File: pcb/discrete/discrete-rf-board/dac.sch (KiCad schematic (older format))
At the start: 19 parts, among them Q20 Q_NPN_BCE

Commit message: Autofill
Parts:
- C71, C72, C77, C78: footprint (none) -> Capacitor_SMD:C_0402_1005Metric; Mouser (none) -> 80-C0402C104M4P
- R45, R46, R47, R48: footprint (none) -> Resistor_SMD:R_0805_2012Metric_Pad1.15x1.40mm_HandSolder; Mouser (none) -> 71-CRCW080515K0FKEBC
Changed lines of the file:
@@
 F 0 "R55" V 3450 2800 50  0000 L CNN
 F 1 "15kR 1%" V 3550 2750 50  0000 L CNN
-F 2 "" H 3350 2850 50  0001 C CNN
+F 2 "Resistor_SMD:R_0805_2012Metric_Pad1.15x1.40mm_HandSolder" H 3350 2850 50  0001 C CNN
 F 3 "~" H 3350 2850 50  0001 C CNN
+F 4 "71-CRCW080515K0FKEBC" H 3350 2850 50  0001 C CNN "Mouser"
 	1    3350 2850
 	0    -1   1    0
@@
 F 0 "R56" V 3450 3100 50  0000 L CNN
 F 1 "15kR 1%" V 3550 3050 50  0000 L CNN
-F 2 "" H 3350 3150 50  0001 C CNN
+F 2 "Resistor_SMD:R_0805_2012Metric_Pad1.15x1.40mm_HandSolder" H 3350 3150 50  0001 C CNN
 F 3 "~" H 3350 3150 50  0001 C CNN
+F 4 "71-CRCW080515K0FKEBC" H 3350 3150 50  0001 C CNN "Mouser"
 	1    3350 3150
 	0    -1   1    0
@@
 F 0 "R57" V 3450 3400 50  0000 L CNN
 F 1 "15kR 1%" V 3550 3350 50  0000 L CNN
-F 2 "" H 3350 3450 50  0001 C CNN
+F 2 "Resistor_SMD:R_0805_2012Metric_Pad1.15x1.40mm_HandSolder" H 3350 3450 50  0001 C CNN
 F 3 "~" H 3350 3450 50  0001 C CNN
+F 4 "71-CRCW080515K0FKEBC" H 3350 3450 50  0001 C CNN "Mouser"
 	1    3350 3450
 	0    -1   1    0
@@
 F 0 "R58" V 3450 3700 50  0000 L CNN
 F 1 "15kR 1%" V 3550 3650 50  0000 L CNN
-F 2 "" H 3350 3750 50  0001 C CNN
+F 2 "Resistor_SMD:R_0805_2012Metric_Pad1.15x1.40mm_HandSolder" H 3350 3750 50  0001 C CNN
 F 3 "~" H 3350 3750 50  0001 C CNN
+F 4 "71-CRCW080515K0FKEBC" H 3350 3750 50  0001 C CNN "Mouser"
 	1    3350 3750
 	0    -1   1    0
@@
 F 0 "C80" H 2210 2220 50  0000 L CNN
 F 1 "0.1 uF" H 2210 2070 50  0000 L CNN
-F 2 "" H 2200 2150 50  0001 C CNN
+F 2 "Capacitor_SMD:C_0402_1005Metric" H 2200 2150 50  0001 C CNN
 F 3 "~" H 2200 2150 50  0001 C CNN
+F 4 "80-C0402C104M4P" H 2200 2150 50  0001 C CNN "Mouser"
 	1    2200 2150
 	1    0    0    -1
@@
 F 0 "C79" H 1810 2220 50  0000 L CNN
 F 1 "0.1 uF" H 1810 2070 50  0000 L CNN
-F 2 "" H 1800 2150 50  0001 C CNN
+F 2 "Capacitor_SMD:C_0402_1005Metric" H 1800 2150 50  0001 C CNN
 F 3 "~" H 1800 2150 50  0001 C CNN
+F 4 "80-C0402C104M4P" H 1800 2150 50  0001 C CNN "Mouser"
 	1    1800 2150
 	1    0    0    -1
@@
 F 0 "C85" H 5510 2220 50  0000 L CNN
 F 1 "0.1 uF" H 5510 2070 50  0000 L CNN
-F 2 "" H 5500 2150 50  0001 C CNN
+F 2 "Capacitor_SMD:C_0402_1005Metric" H 5500 2150 50  0001 C CNN
 F 3 "~" H 5500 2150 50  0001 C CNN
+F 4 "80-C0402C104M4P" H 5500 2150 50  0001 C CNN "Mouser"
 	1    5500 2150
 	-1   0    0    -1
@@
 F 0 "C86" H 5910 2220 50  0000 L CNN
 F 1 "0.1 uF" H 5910 2070 50  0000 L CNN
-F 2 "" H 5900 2150 50  0001 C CNN
+F 2 "Capacitor_SMD:C_0402_1005Metric" H 5900 2150 50  0001 C CNN
 F 3 "~" H 5900 2150 50  0001 C CNN
+F 4 "80-C0402C104M4P" H 5900 2150 50  0001 C CNN "Mouser"
 	1    5900 2150
 	-1   0    0    -1

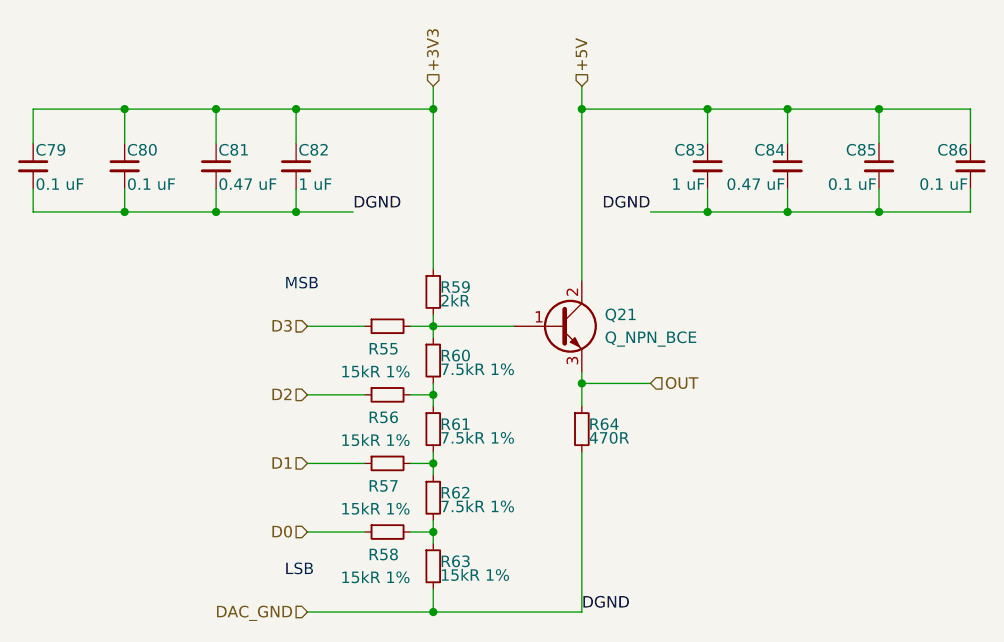
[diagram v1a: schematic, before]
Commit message: Reannotate everything; I'm trying to cut down the number of components
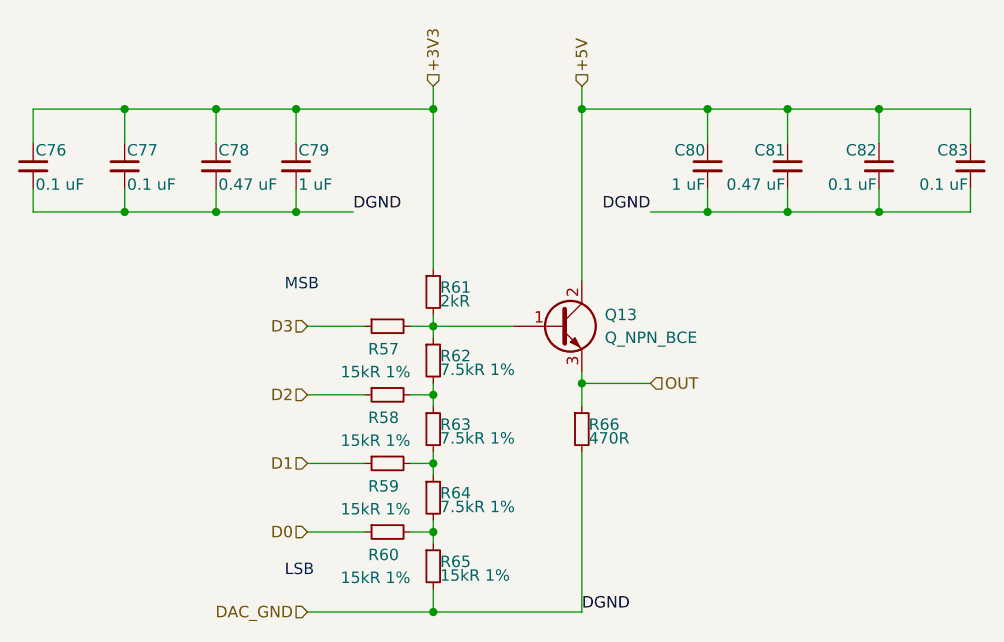
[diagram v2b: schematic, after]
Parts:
- renumbered C71 to C68, C72 to C69, C73 to C70, C74 to C71, C75 to C72, C76 to C73, C77 to C74, C78 to C75, Q20 to Q12, R45 to R47, R46 to R48, R47 to R49, R48 to R50, R49 to R51, R50 to R52, R51 to R53, R52 to R54, R53 to R55, R54 to R56
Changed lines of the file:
@@
 $EndDescr
 $Comp
-L Device:R_Small R49
+L Device:R_Small R51
 U 1 1 5D9928CB
 P 3550 2700
-AR Path="/5CA6B0B3/5D83265A/5D9928CB" Ref="R49"  Part="1"
-AR Path="/5CA6B0B3/5D9A8CAE/5D9928CB" Ref="R59"  Part="1"
-F 0 "R59" H 3580 2720 50  0000 L CNN
+AR Path="/5CA6B0B3/5D83265A/5D9928CB" Ref="R51"  Part="1"
+AR Path="/5CA6B0B3/5D9A8CAE/5D9928CB" Ref="R61"  Part="1"
+F 0 "R61" H 3580 2720 50  0000 L CNN
 F 1 "2kR" H 3580 2660 50  0000 L CNN
 F 2 "" H 3550 2700 50  0001 C CNN
@@
 $EndComp
 $Comp
-L Device:R_Small R50
+L Device:R_Small R52
 U 1 1 5D992BF1
 P 3550 3000
-AR Path="/5CA6B0B3/5D83265A/5D992BF1" Ref="R50"  Part="1"
-AR Path="/5CA6B0B3/5D9A8CAE/5D992BF1" Ref="R60"  Part="1"
-F 0 "R60" H 3580 3020 50  0000 L CNN
+AR Path="/5CA6B0B3/5D83265A/5D992BF1" Ref="R52"  Part="1"
+AR Path="/5CA6B0B3/5D9A8CAE/5D992BF1" Ref="R62"  Part="1"
+F 0 "R62" H 3580 3020 50  0000 L CNN
 F 1 "7.5kR 1%" H 3580 2960 50  0000 L CNN
 F 2 "" H 3550 3000 50  0001 C CNN
@@
 $EndComp
 $Comp
-L Device:R_Small R51
+L Device:R_Small R53
 U 1 1 5D9933B9
 P 3550 3300
-AR Path="/5CA6B0B3/5D83265A/5D9933B9" Ref="R51"  Part="1"
-AR Path="/5CA6B0B3/5D9A8CAE/5D9933B9" Ref="R61"  Part="1"
-F 0 "R61" H 3580 3320 50  0000 L CNN
+AR Path="/5CA6B0B3/5D83265A/5D9933B9" Ref="R53"  Part="1"
+AR Path="/5CA6B0B3/5D9A8CAE/5D9933B9" Ref="R63"  Part="1"
+F 0 "R63" H 3580 3320 50  0000 L CNN
 F 1 "7.5kR 1%" H 3580 3260 50  0000 L CNN
 F 2 "" H 3550 3300 50  0001 C CNN
@@
 $EndComp
 $Comp
-L Device:R_Small R52
+L Device:R_Small R54
 U 1 1 5D993558
 P 3550 3600
-AR Path="/5CA6B0B3/5D83265A/5D993558" Ref="R52"  Part="1"
-AR Path="/5CA6B0B3/5D9A8CAE/5D993558" Ref="R62"  Part="1"
-F 0 "R62" H 3580 3620 50  0000 L CNN
+AR Path="/5CA6B0B3/5D83265A/5D993558" Ref="R54"  Part="1"
+AR Path="/5CA6B0B3/5D9A8CAE/5D993558" Ref="R64"  Part="1"
+F 0 "R64" H 3580 3620 50  0000 L CNN
 F 1 "7.5kR 1%" H 3580 3560 50  0000 L CNN
 F 2 "" H 3550 3600 50  0001 C CNN
@@
 $EndComp
 $Comp
-L Device:R_Small R53
+L Device:R_Small R55
 U 1 1 5D993922
 P 3550 3900
-AR Path="/5CA6B0B3/5D83265A/5D993922" Ref="R53"  Part="1"
-AR Path="/5CA6B0B3/5D9A8CAE/5D993922" Ref="R63"  Part="1"
-F 0 "R63" H 3580 3920 50  0000 L CNN
+AR Path="/5CA6B0B3/5D83265A/5D993922" Ref="R55"  Part="1"
+AR Path="/5CA6B0B3/5D9A8CAE/5D993922" Ref="R65"  Part="1"
+F 0 "R65" H 3580 3920 50  0000 L CNN
 F 1 "15kR 1%" H 3580 3860 50  0000 L CNN
 F 2 "Resistor_SMD:R_0805_2012Metric_Pad1.15x1.40mm_HandSolder" H 3550 3900 50  0001 C CNN
@@
 $EndComp
 $Comp
-L Device:R_Small R45
+L Device:R_Small R47
 U 1 1 5D994F7A
 P 3350 2850
-AR Path="/5CA6B0B3/5D83265A/5D994F7A" Ref="R45"  Part="1"
-AR Path="/5CA6B0B3/5D9A8CAE/5D994F7A" Ref="R55"  Part="1"
-F 0 "R55" V 3450 2800 50  0000 L CNN
+AR Path="/5CA6B0B3/5D83265A/5D994F7A" Ref="R47"  Part="1"
+AR Path="/5CA6B0B3/5D9A8CAE/5D994F7A" Ref="R57"  Part="1"
+F 0 "R57" V 3450 2800 50  0000 L CNN
 F 1 "15kR 1%" V 3550 2750 50  0000 L CNN
 F 2 "Resistor_SMD:R_0805_2012Metric_Pad1.15x1.40mm_HandSolder" H 3350 2850 50  0001 C CNN
@@
 $EndComp
 $Comp
-L Device:R_Small R46
+L Device:R_Small R48
 U 1 1 5D996451
 P 3350 3150
-AR Path="/5CA6B0B3/5D83265A/5D996451" Ref="R46"  Part="1"
-AR Path="/5CA6B0B3/5D9A8CAE/5D996451" Ref="R56"  Part="1"
-F 0 "R56" V 3450 3100 50  0000 L CNN
+AR Path="/5CA6B0B3/5D83265A/5D996451" Ref="R48"  Part="1"
+AR Path="/5CA6B0B3/5D9A8CAE/5D996451" Ref="R58"  Part="1"
+F 0 "R58" V 3450 3100 50  0000 L CNN
 F 1 "15kR 1%" V 3550 3050 50  0000 L CNN
 F 2 "Resistor_SMD:R_0805_2012Metric_Pad1.15x1.40mm_HandSolder" H 3350 3150 50  0001 C CNN
@@
 $EndComp
 $Comp
-L Device:R_Small R47
+L Device:R_Small R49
 U 1 1 5D99666E
 P 3350 3450
-AR Path="/5CA6B0B3/5D83265A/5D99666E" Ref="R47"  Part="1"
-AR Path="/5CA6B0B3/5D9A8CAE/5D99666E" Ref="R57"  Part="1"
-F 0 "R57" V 3450 3400 50  0000 L CNN
+AR Path="/5CA6B0B3/5D83265A/5D99666E" Ref="R49"  Part="1"
+AR Path="/5CA6B0B3/5D9A8CAE/5D99666E" Ref="R59"  Part="1"
+F 0 "R59" V 3450 3400 50  0000 L CNN
 F 1 "15kR 1%" V 3550 3350 50  0000 L CNN
 F 2 "Resistor_SMD:R_0805_2012Metric_Pad1.15x1.40mm_HandSolder" H 3350 3450 50  0001 C CNN
@@
 $EndComp
 $Comp
-L Device:R_Small R48
+L Device:R_Small R50
 U 1 1 5D99690F
 P 3350 3750
-AR Path="/5CA6B0B3/5D83265A/5D99690F" Ref="R48"  Part="1"
-AR Path="/5CA6B0B3/5D9A8CAE/5D99690F" Ref="R58"  Part="1"
-F 0 "R58" V 3450 3700 50  0000 L CNN
+AR Path="/5CA6B0B3/5D83265A/5D99690F" Ref="R50"  Part="1"
+AR Path="/5CA6B0B3/5D9A8CAE/5D99690F" Ref="R60"  Part="1"
+F 0 "R60" V 3450 3700 50  0000 L CNN
 F 1 "15kR 1%" V 3550 3650 50  0000 L CNN
 F 2 "Resistor_SMD:R_0805_2012Metric_Pad1.15x1.40mm_HandSolder" H 3350 3750 50  0001 C CNN
@@
 	3550 3750 3550 3700
 $Comp
-L Device:Q_NPN_BCE Q20
+L Device:Q_NPN_BCE Q12
 U 1 1 5D998D16
 P 4100 2850
-AR Path="/5CA6B0B3/5D83265A/5D998D16" Ref="Q20"  Part="1"
-AR Path="/5CA6B0B3/5D9A8CAE/5D998D16" Ref="Q21"  Part="1"
-F 0 "Q21" H 4300 2900 50  0000 L CNN
+AR Path="/5CA6B0B3/5D83265A/5D998D16" Ref="Q12"  Part="1"
+AR Path="/5CA6B0B3/5D9A8CAE/5D998D16" Ref="Q13"  Part="1"
+F 0 "Q13" H 4300 2900 50  0000 L CNN
 F 1 "Q_NPN_BCE" H 4300 2800 50  0000 L CNN
 F 2 "" H 4300 2950 50  0001 C CNN
@@
 	3550 1800 3550 1900
 $Comp
-L Device:R_Small R54
+L Device:R_Small R56
 U 1 1 5D99E2FA
 P 4200 3300
-AR Path="/5CA6B0B3/5D83265A/5D99E2FA" Ref="R54"  Part="1"
-AR Path="/5CA6B0B3/5D9A8CAE/5D99E2FA" Ref="R64"  Part="1"
-F 0 "R64" H 4230 3320 50  0000 L CNN
+AR Path="/5CA6B0B3/5D83265A/5D99E2FA" Ref="R56"  Part="1"
+AR Path="/5CA6B0B3/5D9A8CAE/5D99E2FA" Ref="R66"  Part="1"
+F 0 "R66" H 4230 3320 50  0000 L CNN
 F 1 "470R" H 4230 3260 50  0000 L CNN
 F 2 "" H 4200 3300 50  0001 C CNN
@@
 Connection ~ 3550 4100
 $Comp
-L Device:C_Small C74
+L Device:C_Small C71
 U 1 1 5DC04556
 P 2950 2150
-AR Path="/5CA6B0B3/5D83265A/5DC04556" Ref="C74"  Part="1"
-AR Path="/5CA6B0B3/5D9A8CAE/5DC04556" Ref="C82"  Part="1"
-F 0 "C82" H 2960 2220 50  0000 L CNN
+AR Path="/5CA6B0B3/5D83265A/5DC04556" Ref="C71"  Part="1"
+AR Path="/5CA6B0B3/5D9A8CAE/5DC04556" Ref="C79"  Part="1"
+F 0 "C79" H 2960 2220 50  0000 L CNN
 F 1 "1 uF" H 2960 2070 50  0000 L CNN
 F 2 "" H 2950 2150 50  0001 C CNN
@@
 $EndComp
 $Comp
-L Device:C_Small C73
+L Device:C_Small C70
 U 1 1 5DC04C84
 P 2600 2150
-AR Path="/5CA6B0B3/5D83265A/5DC04C84" Ref="C73"  Part="1"
-AR Path="/5CA6B0B3/5D9A8CAE/5DC04C84" Ref="C81"  Part="1"
-F 0 "C81" H 2610 2220 50  0000 L CNN
+AR Path="/5CA6B0B3/5D83265A/5DC04C84" Ref="C70"  Part="1"
+AR Path="/5CA6B0B3/5D9A8CAE/5DC04C84" Ref="C78"  Part="1"
+F 0 "C78" H 2610 2220 50  0000 L CNN
 F 1 "0.47 uF" H 2610 2070 50  0000 L CNN
 F 2 "Capacitor_SMD:C_0402_1005Metric" H 2600 2150 50  0001 C CNN
@@
 $EndComp
 $Comp
-L Device:C_Small C72
+L Device:C_Small C69
 U 1 1 5DC04F33
 P 2200 2150
-AR Path="/5CA6B0B3/5D83265A/5DC04F33" Ref="C72"  Part="1"
-AR Path="/5CA6B0B3/5D9A8CAE/5DC04F33" Ref="C80"  Part="1"
-F 0 "C80" H 2210 2220 50  0000 L CNN
+AR Path="/5CA6B0B3/5D83265A/5DC04F33" Ref="C69"  Part="1"
+AR Path="/5CA6B0B3/5D9A8CAE/5DC04F33" Ref="C77"  Part="1"
+F 0 "C77" H 2210 2220 50  0000 L CNN
 F 1 "0.1 uF" H 2210 2070 50  0000 L CNN
 F 2 "Capacitor_SMD:C_0402_1005Metric" H 2200 2150 50  0001 C CNN
@@
 $EndComp
 $Comp
-L Device:C_Small C71
+L Device:C_Small C68
 U 1 1 5DC05279
 P 1800 2150
-AR Path="/5CA6B0B3/5D83265A/5DC05279" Ref="C71"  Part="1"
-AR Path="/5CA6B0B3/5D9A8CAE/5DC05279" Ref="C79"  Part="1"
-F 0 "C79" H 1810 2220 50  0000 L CNN
+AR Path="/5CA6B0B3/5D83265A/5DC05279" Ref="C68"  Part="1"
+AR Path="/5CA6B0B3/5D9A8CAE/5DC05279" Ref="C76"  Part="1"
+F 0 "C76" H 1810 2220 50  0000 L CNN
 F 1 "0.1 uF" H 1810 2070 50  0000 L CNN
 F 2 "Capacitor_SMD:C_0402_1005Metric" H 1800 2150 50  0001 C CNN
@@
 	2950 2350 2600 2350
 $Comp
-L Device:C_Small C75
+L Device:C_Small C72
 U 1 1 5DC0F871
 P 4750 2150
-AR Path="/5CA6B0B3/5D83265A/5DC0F871" Ref="C75"  Part="1"
-AR Path="/5CA6B0B3/5D9A8CAE/5DC0F871" Ref="C83"  Part="1"
-F 0 "C83" H 4760 2220 50  0000 L CNN
+AR Path="/5CA6B0B3/5D83265A/5DC0F871" Ref="C72"  Part="1"
+AR Path="/5CA6B0B3/5D9A8CAE/5DC0F871" Ref="C80"  Part="1"
+F 0 "C80" H 4760 2220 50  0000 L CNN
 F 1 "1 uF" H 4760 2070 50  0000 L CNN
 F 2 "" H 4750 2150 50  0001 C CNN
@@
 $EndComp
 $Comp
-L Device:C_Small C76
+L Device:C_Small C73
 U 1 1 5DC0F877
 P 5100 2150
-AR Path="/5CA6B0B3/5D83265A/5DC0F877" Ref="C76"  Part="1"
-AR Path="/5CA6B0B3/5D9A8CAE/5DC0F877" Ref="C84"  Part="1"
-F 0 "C84" H 5110 2220 50  0000 L CNN
+AR Path="/5CA6B0B3/5D83265A/5DC0F877" Ref="C73"  Part="1"
+AR Path="/5CA6B0B3/5D9A8CAE/5DC0F877" Ref="C81"  Part="1"
+F 0 "C81" H 5110 2220 50  0000 L CNN
 F 1 "0.47 uF" H 5110 2070 50  0000 L CNN
 F 2 "Capacitor_SMD:C_0402_1005Metric" H 5100 2150 50  0001 C CNN
@@
 $EndComp
 $Comp
-L Device:C_Small C77
+L Device:C_Small C74
 U 1 1 5DC0F87D
 P 5500 2150
-AR Path="/5CA6B0B3/5D83265A/5DC0F87D" Ref="C77"  Part="1"
-AR Path="/5CA6B0B3/5D9A8CAE/5DC0F87D" Ref="C85"  Part="1"
-F 0 "C85" H 5510 2220 50  0000 L CNN
+AR Path="/5CA6B0B3/5D83265A/5DC0F87D" Ref="C74"  Part="1"
+AR Path="/5CA6B0B3/5D9A8CAE/5DC0F87D" Ref="C82"  Part="1"
+F 0 "C82" H 5510 2220 50  0000 L CNN
 F 1 "0.1 uF" H 5510 2070 50  0000 L CNN
 F 2 "Capacitor_SMD:C_0402_1005Metric" H 5500 2150 50  0001 C CNN
@@
 $EndComp
 $Comp
-L Device:C_Small C78
+L Device:C_Small C75
 U 1 1 5DC0F883
 P 5900 2150
-AR Path="/5CA6B0B3/5D83265A/5DC0F883" Ref="C78"  Part="1"
-AR Path="/5CA6B0B3/5D9A8CAE/5DC0F883" Ref="C86"  Part="1"
-F 0 "C86" H 5910 2220 50  0000 L CNN
+AR Path="/5CA6B0B3/5D83265A/5DC0F883" Ref="C75"  Part="1"
+AR Path="/5CA6B0B3/5D9A8CAE/5DC0F883" Ref="C83"  Part="1"
+F 0 "C83" H 5910 2220 50  0000 L CNN
 F 1 "0.1 uF" H 5910 2070 50  0000 L CNN
 F 2 "Capacitor_SMD:C_0402_1005Metric" H 5900 2150 50  0001 C CNN

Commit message: Footprint a lot of stuff; save before autofill
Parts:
- C71: footprint (none) -> Capacitor_SMD:C_0402_1005Metric; Mouser (none) -> 963-EMK105BJ105KV-F
- R51: footprint (none) -> Resistor_SMD:R_0402_1005Metric; Mouser (none) -> 603-RC0402FR-072KL
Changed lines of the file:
@@
 AR Path="/5CA6B0B3/5D83265A/5D9928CB" Ref="R51"  Part="1"
 AR Path="/5CA6B0B3/5D9A8CAE/5D9928CB" Ref="R61"  Part="1"
-F 0 "R61" H 3580 2720 50  0000 L CNN
+F 0 "R51" H 3580 2720 50  0000 L CNN
 F 1 "2kR" H 3580 2660 50  0000 L CNN
-F 2 "" H 3550 2700 50  0001 C CNN
+F 2 "Resistor_SMD:R_0402_1005Metric" H 3550 2700 50  0001 C CNN
 F 3 "~" H 3550 2700 50  0001 C CNN
+F 4 "603-RC0402FR-072KL" H 3550 2700 50  0001 C CNN "Mouser"
 	1    3550 2700
 	1    0    0    -1
@@
 AR Path="/5CA6B0B3/5D83265A/5D992BF1" Ref="R52"  Part="1"
 AR Path="/5CA6B0B3/5D9A8CAE/5D992BF1" Ref="R62"  Part="1"
-F 0 "R62" H 3580 3020 50  0000 L CNN
+F 0 "R52" H 3580 3020 50  0000 L CNN
 F 1 "7.5kR 1%" H 3580 2960 50  0000 L CNN
 F 2 "" H 3550 3000 50  0001 C CNN
@@
 AR Path="/5CA6B0B3/5D83265A/5D9933B9" Ref="R53"  Part="1"
 AR Path="/5CA6B0B3/5D9A8CAE/5D9933B9" Ref="R63"  Part="1"
-F 0 "R63" H 3580 3320 50  0000 L CNN
+F 0 "R53" H 3580 3320 50  0000 L CNN
 F 1 "7.5kR 1%" H 3580 3260 50  0000 L CNN
 F 2 "" H 3550 3300 50  0001 C CNN
@@
 AR Path="/5CA6B0B3/5D83265A/5D993558" Ref="R54"  Part="1"
 AR Path="/5CA6B0B3/5D9A8CAE/5D993558" Ref="R64"  Part="1"
-F 0 "R64" H 3580 3620 50  0000 L CNN
+F 0 "R54" H 3580 3620 50  0000 L CNN
 F 1 "7.5kR 1%" H 3580 3560 50  0000 L CNN
 F 2 "" H 3550 3600 50  0001 C CNN
@@
 AR Path="/5CA6B0B3/5D83265A/5D993922" Ref="R55"  Part="1"
 AR Path="/5CA6B0B3/5D9A8CAE/5D993922" Ref="R65"  Part="1"
-F 0 "R65" H 3580 3920 50  0000 L CNN
+F 0 "R55" H 3580 3920 50  0000 L CNN
 F 1 "15kR 1%" H 3580 3860 50  0000 L CNN
 F 2 "Resistor_SMD:R_0805_2012Metric_Pad1.15x1.40mm_HandSolder" H 3550 3900 50  0001 C CNN
@@
 AR Path="/5CA6B0B3/5D83265A/5D994F7A" Ref="R47"  Part="1"
 AR Path="/5CA6B0B3/5D9A8CAE/5D994F7A" Ref="R57"  Part="1"
-F 0 "R57" V 3450 2800 50  0000 L CNN
+F 0 "R47" V 3450 2800 50  0000 L CNN
 F 1 "15kR 1%" V 3550 2750 50  0000 L CNN
 F 2 "Resistor_SMD:R_0805_2012Metric_Pad1.15x1.40mm_HandSolder" H 3350 2850 50  0001 C CNN
@@
 AR Path="/5CA6B0B3/5D83265A/5D996451" Ref="R48"  Part="1"
 AR Path="/5CA6B0B3/5D9A8CAE/5D996451" Ref="R58"  Part="1"
-F 0 "R58" V 3450 3100 50  0000 L CNN
+F 0 "R48" V 3450 3100 50  0000 L CNN
 F 1 "15kR 1%" V 3550 3050 50  0000 L CNN
 F 2 "Resistor_SMD:R_0805_2012Metric_Pad1.15x1.40mm_HandSolder" H 3350 3150 50  0001 C CNN
@@
 AR Path="/5CA6B0B3/5D83265A/5D99666E" Ref="R49"  Part="1"
 AR Path="/5CA6B0B3/5D9A8CAE/5D99666E" Ref="R59"  Part="1"
-F 0 "R59" V 3450 3400 50  0000 L CNN
+F 0 "R49" V 3450 3400 50  0000 L CNN
 F 1 "15kR 1%" V 3550 3350 50  0000 L CNN
 F 2 "Resistor_SMD:R_0805_2012Metric_Pad1.15x1.40mm_HandSolder" H 3350 3450 50  0001 C CNN
@@
 AR Path="/5CA6B0B3/5D83265A/5D99690F" Ref="R50"  Part="1"
 AR Path="/5CA6B0B3/5D9A8CAE/5D99690F" Ref="R60"  Part="1"
-F 0 "R60" V 3450 3700 50  0000 L CNN
+F 0 "R50" V 3450 3700 50  0000 L CNN
 F 1 "15kR 1%" V 3550 3650 50  0000 L CNN
 F 2 "Resistor_SMD:R_0805_2012Metric_Pad1.15x1.40mm_HandSolder" H 3350 3750 50  0001 C CNN
@@
 AR Path="/5CA6B0B3/5D83265A/5D998D16" Ref="Q12"  Part="1"
 AR Path="/5CA6B0B3/5D9A8CAE/5D998D16" Ref="Q13"  Part="1"
-F 0 "Q13" H 4300 2900 50  0000 L CNN
+F 0 "Q12" H 4300 2900 50  0000 L CNN
 F 1 "Q_NPN_BCE" H 4300 2800 50  0000 L CNN
 F 2 "" H 4300 2950 50  0001 C CNN
@@
 AR Path="/5CA6B0B3/5D83265A/5D99E2FA" Ref="R56"  Part="1"
 AR Path="/5CA6B0B3/5D9A8CAE/5D99E2FA" Ref="R66"  Part="1"
-F 0 "R66" H 4230 3320 50  0000 L CNN
+F 0 "R56" H 4230 3320 50  0000 L CNN
 F 1 "470R" H 4230 3260 50  0000 L CNN
 F 2 "" H 4200 3300 50  0001 C CNN
@@
 AR Path="/5CA6B0B3/5D83265A/5DC04556" Ref="C71"  Part="1"
 AR Path="/5CA6B0B3/5D9A8CAE/5DC04556" Ref="C79"  Part="1"
-F 0 "C79" H 2960 2220 50  0000 L CNN
+F 0 "C71" H 2960 2220 50  0000 L CNN
 F 1 "1 uF" H 2960 2070 50  0000 L CNN
-F 2 "" H 2950 2150 50  0001 C CNN
+F 2 "Capacitor_SMD:C_0402_1005Metric" H 2950 2150 50  0001 C CNN
 F 3 "~" H 2950 2150 50  0001 C CNN
+F 4 "963-EMK105BJ105KV-F" H 2950 2150 50  0001 C CNN "Mouser"
 	1    2950 2150
 	1    0    0    -1
@@
 AR Path="/5CA6B0B3/5D83265A/5DC04C84" Ref="C70"  Part="1"
 AR Path="/5CA6B0B3/5D9A8CAE/5DC04C84" Ref="C78"  Part="1"
-F 0 "C78" H 2610 2220 50  0000 L CNN
+F 0 "C70" H 2610 2220 50  0000 L CNN
 F 1 "0.47 uF" H 2610 2070 50  0000 L CNN
 F 2 "Capacitor_SMD:C_0402_1005Metric" H 2600 2150 50  0001 C CNN
@@
 AR Path="/5CA6B0B3/5D83265A/5DC04F33" Ref="C69"  Part="1"
 AR Path="/5CA6B0B3/5D9A8CAE/5DC04F33" Ref="C77"  Part="1"
-F 0 "C77" H 2210 2220 50  0000 L CNN
+F 0 "C69" H 2210 2220 50  0000 L CNN
 F 1 "0.1 uF" H 2210 2070 50  0000 L CNN
 F 2 "Capacitor_SMD:C_0402_1005Metric" H 2200 2150 50  0001 C CNN
@@
 AR Path="/5CA6B0B3/5D83265A/5DC05279" Ref="C68"  Part="1"
 AR Path="/5CA6B0B3/5D9A8CAE/5DC05279" Ref="C76"  Part="1"
-F 0 "C76" H 1810 2220 50  0000 L CNN
+F 0 "C68" H 1810 2220 50  0000 L CNN
 F 1 "0.1 uF" H 1810 2070 50  0000 L CNN
 F 2 "Capacitor_SMD:C_0402_1005Metric" H 1800 2150 50  0001 C CNN
@@
 AR Path="/5CA6B0B3/5D83265A/5DC0F871" Ref="C72"  Part="1"
 AR Path="/5CA6B0B3/5D9A8CAE/5DC0F871" Ref="C80"  Part="1"
-F 0 "C80" H 4760 2220 50  0000 L CNN
+F 0 "C72" H 4760 2220 50  0000 L CNN
 F 1 "1 uF" H 4760 2070 50  0000 L CNN
 F 2 "" H 4750 2150 50  0001 C CNN
@@
 AR Path="/5CA6B0B3/5D83265A/5DC0F877" Ref="C73"  Part="1"
 AR Path="/5CA6B0B3/5D9A8CAE/5DC0F877" Ref="C81"  Part="1"
-F 0 "C81" H 5110 2220 50  0000 L CNN
+F 0 "C73" H 5110 2220 50  0000 L CNN
 F 1 "0.47 uF" H 5110 2070 50  0000 L CNN
 F 2 "Capacitor_SMD:C_0402_1005Metric" H 5100 2150 50  0001 C CNN
@@
 AR Path="/5CA6B0B3/5D83265A/5DC0F87D" Ref="C74"  Part="1"
 AR Path="/5CA6B0B3/5D9A8CAE/5DC0F87D" Ref="C82"  Part="1"
-F 0 "C82" H 5510 2220 50  0000 L CNN
+F 0 "C74" H 5510 2220 50  0000 L CNN
 F 1 "0.1 uF" H 5510 2070 50  0000 L CNN
 F 2 "Capacitor_SMD:C_0402_1005Metric" H 5500 2150 50  0001 C CNN
@@
 AR Path="/5CA6B0B3/5D83265A/5DC0F883" Ref="C75"  Part="1"
 AR Path="/5CA6B0B3/5D9A8CAE/5DC0F883" Ref="C83"  Part="1"
-F 0 "C83" H 5910 2220 50  0000 L CNN
+F 0 "C75" H 5910 2220 50  0000 L CNN
 F 1 "0.1 uF" H 5910 2070 50  0000 L CNN
 F 2 "Capacitor_SMD:C_0402_1005Metric" H 5900 2150 50  0001 C CNN

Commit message: Autofill
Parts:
- C72: footprint (none) -> Capacitor_SMD:C_0402_1005Metric; Mouser (none) -> 963-EMK105BJ105KV-F
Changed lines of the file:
@@
 F 0 "C72" H 4760 2220 50  0000 L CNN
 F 1 "1 uF" H 4760 2070 50  0000 L CNN
-F 2 "" H 4750 2150 50  0001 C CNN
+F 2 "Capacitor_SMD:C_0402_1005Metric" H 4750 2150 50  0001 C CNN
 F 3 "~" H 4750 2150 50  0001 C CNN
+F 4 "963-EMK105BJ105KV-F" H 4750 2150 50  0001 C CNN "Mouser"
 	1    4750 2150
 	-1   0    0    -1

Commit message: Add in a couple more components, save before autofill
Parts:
- R56: footprint (none) -> Resistor_SMD:R_0402_1005Metric; Mouser (none) -> 603-RC0402JR-13470RL
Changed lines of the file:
@@
 F 0 "R56" H 4230 3320 50  0000 L CNN
 F 1 "470R" H 4230 3260 50  0000 L CNN
-F 2 "" H 4200 3300 50  0001 C CNN
+F 2 "Resistor_SMD:R_0402_1005Metric" H 4200 3300 50  0001 C CNN
 F 3 "~" H 4200 3300 50  0001 C CNN
+F 4 "603-RC0402JR-13470RL" H 4200 3300 50  0001 C CNN "Mouser"
 	1    4200 3300
 	1    0    0    -1

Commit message: Footprint more stuff
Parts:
- R52: footprint (none) -> Resistor_SMD:R_0402_1005Metric; Mouser (none) -> 667-ERJ-2RKF7501X
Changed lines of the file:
@@
 F 0 "R52" H 3580 3020 50  0000 L CNN
 F 1 "7.5kR 1%" H 3580 2960 50  0000 L CNN
-F 2 "" H 3550 3000 50  0001 C CNN
+F 2 "Resistor_SMD:R_0402_1005Metric" H 3550 3000 50  0001 C CNN
 F 3 "~" H 3550 3000 50  0001 C CNN
+F 4 "667-ERJ-2RKF7501X" H 3550 3000 50  0001 C CNN "Mouser"
 	1    3550 3000
 	1    0    0    -1
